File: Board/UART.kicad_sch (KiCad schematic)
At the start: 24 parts, among them IC31 MAX232, IC32 MAX232, IC33 UARTPLCC, IC34 7406N, IC35 74138N, X3 M09HPS

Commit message: ultipet 1.1a board
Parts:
- removed IC33: UARTPLCC, cbm_ultipet_v1:PLCC44, symbol cbm_ultipet_v1-eagle-import:UARTPLCC
- removed JP21, JP22, JP23, JP25: JP2E, cbm_ultipet_v1:JP2, symbol cbm_ultipet_v1-eagle-import:JP2E
- removed R103: 10k, cbm_ultipet_v1:0207_10, symbol cbm_ultipet_v1-eagle-import:R-EU_0207/10
- added unit 5 of IC34
- added IC6: TL16C752C, Package_QFP:TQFP-48_7x7mm_P0.5mm, symbol TL16C752C:TL16C752C
- added U$2: JP5, cbm_ultipet_v1:JP5, symbol cbm_ultipet_v1-eagle-import:JP5
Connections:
- net /SEL1 is gone; now on net GND: IC35.4 (G2A)
- net BCTS is gone; now on net LCTS: U$27.2
- net BSIN is gone; now on net LRX: U$27.4
- net /BIRQ: now also IC34.10 (O)
- net BA0: now also IC6.28 (A0)
- net BA1: now also IC6.27 (A1)
- net BA2: now also IC6.26 (A2)
- net BD0: now also IC6.44 (D0)
- net BD1: now also IC6.45 (D1)
- net BD2: now also IC6.46 (D2)
- net BD3: now also IC6.47 (D3)
- net BD4: now also IC6.48 (D4)
- net BD5: now also IC6.1 (D5)
- net BD6: now also IC6.2 (D6)
- net BD7: now also IC6.3 (D7)
- net GND: now also IC6.17 (GND), U$2.1
- net LCTS: now also IC6.38 (/CTSA)
- net LDCD: now also IC6.40 (/CDA)
- net LDSR: now also IC6.39 (/DSRA)
- net LDTR: now also IC6.34 (/DTRA)
- net LRTS: now also IC6.33 (/RTSA)
- net LRX: now also IC6.5 (RXA)
- net LTX: now also IC6.7 (TXA)
- net VCC: now also IC6.42 (VCC)
- net PULLUP_UART: now reaches IC34.4 (O)
- net PULLUP_UART: now also IC6.36 (RESET)
- net /QRD: now reaches IC35.11 (Y4)
- net /QRD: now also IC6.15 (/IOW)
- net /QWR: now reaches IC35.10 (Y5)
- net /QWR: now also IC6.19 (/IOR)
- net at IC34.1 (I): now also IC6.30 (INTA)
- net SERCLK: no longer names the net of QG3.8 (OUT)
- net SERCLK: now also IC6.13 (XTALI)
- new net: IC34.11 (I), IC6.29 (INTB)
- new net OPENHIGH: IC6.16 (/CDB), IC6.20 (/DSRB), IC6.21 (/RIB), IC6.41 (/RIA)
- new net RCTS: IC6.23 (/CTSB), U$2.2
- new net RRTS: IC6.22 (/RTSB), U$2.5
- new net RRX: IC6.4 (RXB), U$2.4
- new net RTX: IC6.8 (TXB), U$2.3
- new net /SEL1: IC6.10 (/CSA)
- new net /SEL2: IC6.11 (/CSB)
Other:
- note added: "$e818-$e81f $e828-$e82f"
- note added: "1.1A: - Switch to DUAL UART to provide 2nd 5V RS232 (shared w/ UEXT) - replace pullup on UART /RES with RN7"
- note added: "CBM-ULTIPET-V1.1A"
- note added: "CBM-ULTIPET-V1.1A-20240525"
- note added: "RS232<->USB breakout board connector - Do not use if UEXT is used!"
- note added: "RS232<->USB breakout board connector - Remove MAX232 if used!"
- note removed: "$e818-$e81f"
- note removed: "- Changed UART to PLCC as DIP is unobtainable"
- note removed: "CBM-ULTIPET-V1.0A"
- note removed: "CBM-ULTIPET-V1.0A-20240122"
- note removed: "RS232<->USB breakout board connector"
- moved on the sheet: C134, C135, C137, C139, C84, C86, C87, C88, C89, C90, C91, IC31A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

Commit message: diverse fixes
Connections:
- net GND: now also IC6.16 (/CDB), IC6.20 (/DSRB)
- net OPENHIGH: no longer IC6.16 (/CDB), IC6.20 (/DSRB)
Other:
- note added: "1.1A: - Switch to DUAL UART to provide 2nd 5V RS232 (shared w/ UEXT) - replace pullup on UART /RES with RN7 1.2A: - set /DSRB and /CDB to lo instead of hi"
- note added: "CBM-ULTIPET-V1.2A"
- note added: "CBM-ULTIPET-V1.2A-20241010"
- note removed: "1.1A: - Switch to DUAL UART to provide 2nd 5V RS232 (shared w/ UEXT) - replace pullup on UART /RES with RN7"
- note removed: "CBM-ULTIPET-V1.1A"
- note removed: "CBM-ULTIPET-V1.1A-20240525"
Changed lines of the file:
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@@
 	)
 	(junction
+		(at 220.98 179.07)
+		(diameter 0)
+		(color 0 0 0 0)
+	)
+	(junction
 		(at 269.24 176.53)
 		(diameter 0)
@@
 	)
 	(junction
-		(at 217.17 173.99)
-		(diameter 0)
-		(color 0 0 0 0)
-	)
-	(junction
 		(at 273.05 40.64)
 		(diameter 0)
@@
 		(color 0 0 0 0)
 	)
-	(junction
-		(at 217.17 179.07)
-		(diameter 0)
-		(color 0 0 0 0)
-	)
 	(bus_entry
 		(at 153.67 143.51)
@@
 	(wire
 		(pts
-			(xy 217.17 181.61) (xy 217.17 179.07)
+			(xy 220.98 179.07) (xy 220.98 194.31)
+		)
+		(stroke
+			(width 0)
+			(type default)
+		)
+	)
+	(wire
+		(pts
+			(xy 217.17 168.91) (xy 217.17 181.61)
 		)
 		(stroke
@@
 	(wire
 		(pts
-			(xy 217.17 179.07) (xy 217.17 173.99)
-		)
-		(stroke
-			(width 0)
-			(type default)
-		)
-	)
-	(wire
-		(pts
 			(xy 298.45 96.52) (xy 280.67 96.52)
 		)
@@
 	(wire
 		(pts
+			(xy 208.28 179.07) (xy 220.98 179.07)
+		)
+		(stroke
+			(width 0)
+			(type default)
+		)
+	)
+	(wire
+		(pts
 			(xy 288.29 71.12) (xy 288.29 58.42)
 		)
@@
 	(wire
 		(pts
+			(xy 220.98 173.99) (xy 220.98 179.07)
+		)
+		(stroke
+			(width 0)
+			(type default)
+		)
+	)
+	(wire
+		(pts
 			(xy 219.71 71.12) (xy 227.33 71.12)
 		)
@@
 		)
 	)
-	(wire
-		(pts
-			(xy 217.17 173.99) (xy 217.17 168.91)
-		)
-		(stroke
-			(width 0)
-			(type default)
-		)
-	)
 	(bus
 		(pts
@@
 	(wire
 		(pts
-			(xy 208.28 173.99) (xy 217.17 173.99)
-		)
-		(stroke
-			(width 0)
-			(type default)
-		)
-	)
-	(wire
-		(pts
 			(xy 227.33 38.1) (xy 227.33 40.64)
 		)
@@
 		)
 	)
-	(wire
-		(pts
-			(xy 208.28 179.07) (xy 217.17 179.07)
-		)
-		(stroke
-			(width 0)
-			(type default)
-		)
-	)
 	(bus
 		(pts
@@
 	(wire
 		(pts
+			(xy 208.28 173.99) (xy 220.98 173.99)
+		)
+		(stroke
+			(width 0)
+			(type default)
+		)
+	)
+	(wire
+		(pts
 			(xy 86.36 214.63) (xy 104.14 214.63)
 		)
@@
 		)
 	)
-	(text "CBM-ULTIPET-V1.1A\n"
+	(text "CBM-ULTIPET-V1.2A\n"
 		(exclude_from_sim no)
 		(at 294.64 224.028 0)
@@
 		)
 	)
-	(text "CBM-ULTIPET-V1.1A-20240525"
+	(text "CBM-ULTIPET-V1.2A-20241010"
 		(exclude_from_sim no)
 		(at 303.276 243.84 0)
@@
 		)
 	)
-	(text "1.1A:\n- Switch to DUAL UART to provide 2nd\n  5V RS232 (shared w/ UEXT)\n- replace pullup on UART /RES \n  with RN7"
+	(text "1.1A:\n- Switch to DUAL UART to provide 2nd\n  5V RS232 (shared w/ UEXT)\n- replace pullup on UART /RES \n  with RN7\n1.2A:\n- set /DSRB and /CDB to lo instead of hi"
 		(exclude_from_sim no)
-		(at 310.896 141.986 0)
+		(at 300.482 144.018 0)
 		(effects
 			(font
@@
 					(unit 1)
 				)
+			)
+		)
+	)
+	(symbol
+		(lib_id "cbm_ultipet_v1-eagle-import:GND")
+		(at 220.98 196.85 0)
+		(unit 1)
+		(exclude_from_sim no)
+		(in_bom yes)
+		(on_board yes)
+		(dnp no)
+		(property "Reference" "#GND0143"
+			(at 220.98 196.85 0)
+			(effects
+				(font
+					(size 1.27 1.27)
+				)
+				(hide yes)
+			)
+		)
+		(property "Value" "GND"
+			(at 218.44 199.39 0)
+			(effects
+				(font
+					(size 1.778 1.5113)
+				)
+				(justify left bottom)
+			)
+		)
+		(property "Footprint" ""
+			(at 220.98 196.85 0)
+			(effects
+				(font
+					(size 1.27 1.27)
+				)
+				(hide yes)
+			)
+		)
+		(property "Datasheet" ""
+			(at 220.98 196.85 0)
+			(effects
+				(font
+					(size 1.27 1.27)
+				)
+				(hide yes)
+			)
+		)
+		(property "Description" ""
+			(at 220.98 196.85 0)
+			(effects
+				(font
+					(size 1.27 1.27)
+				)
+				(hide yes)
+			)
+		)
+		(pin "1"
+		)
+		(instances
+			(project "cbm_ultipet_v1"
+				(path "/4dd2dd78-173f-4b46-8cce-4ed940435c94/511b245b-0d04-40fa-b689-60e442c438dc"
+					(reference "#GND0143")
+					(unit 1)
+				)

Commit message: various fixes as documented in github issues
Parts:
- added R12, R5: 10k, cbm_ultipet_v1:0207_10, symbol cbm_ultipet_v1-eagle-import:R-EU_0207/10
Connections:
- net GND: now also R12.1, R5.1
- net at IC34.1 (I), IC6.30 (INTA): now also R12.2
- net at IC34.11 (I), IC6.29 (INTB): now also R5.2
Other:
- note added: "1.1A: - Switch to DUAL UART to provide 2nd 5V RS232 (shared w/ UEXT) - replace pullup on UART /RES with RN7 1.2A: - set /DSRB and /CDB to lo instead of hi . add pulldowns to INTA and INTB so high-Z does not trigger IRQ"
- note added: "CBM-ULTIPET-V1.2A-20241013"
- note removed: "1.1A: - Switch to DUAL UART to provide 2nd 5V RS232 (shared w/ UEXT) - replace pullup on UART /RES with RN7 1.2A: - set /DSRB and /CDB to lo instead of hi"
- note removed: "CBM-ULTIPET-V1.2A-20241010"

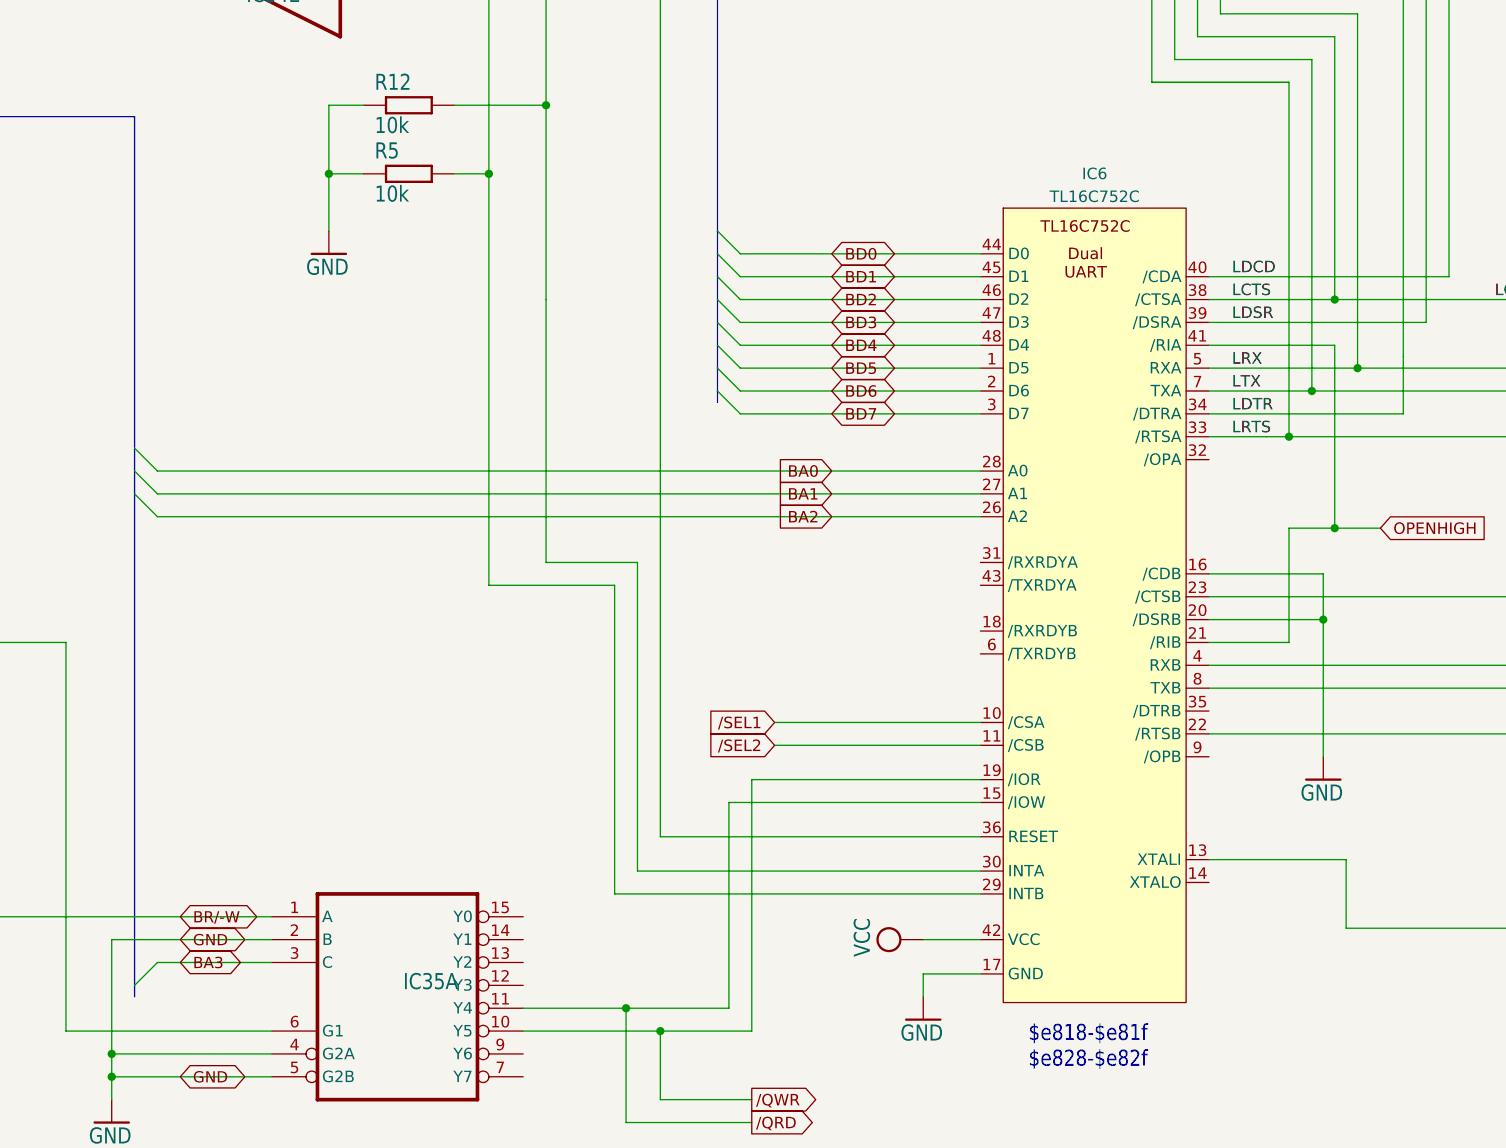
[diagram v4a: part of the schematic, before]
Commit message: replace some ultipet specific TQFP with easier to solder parts
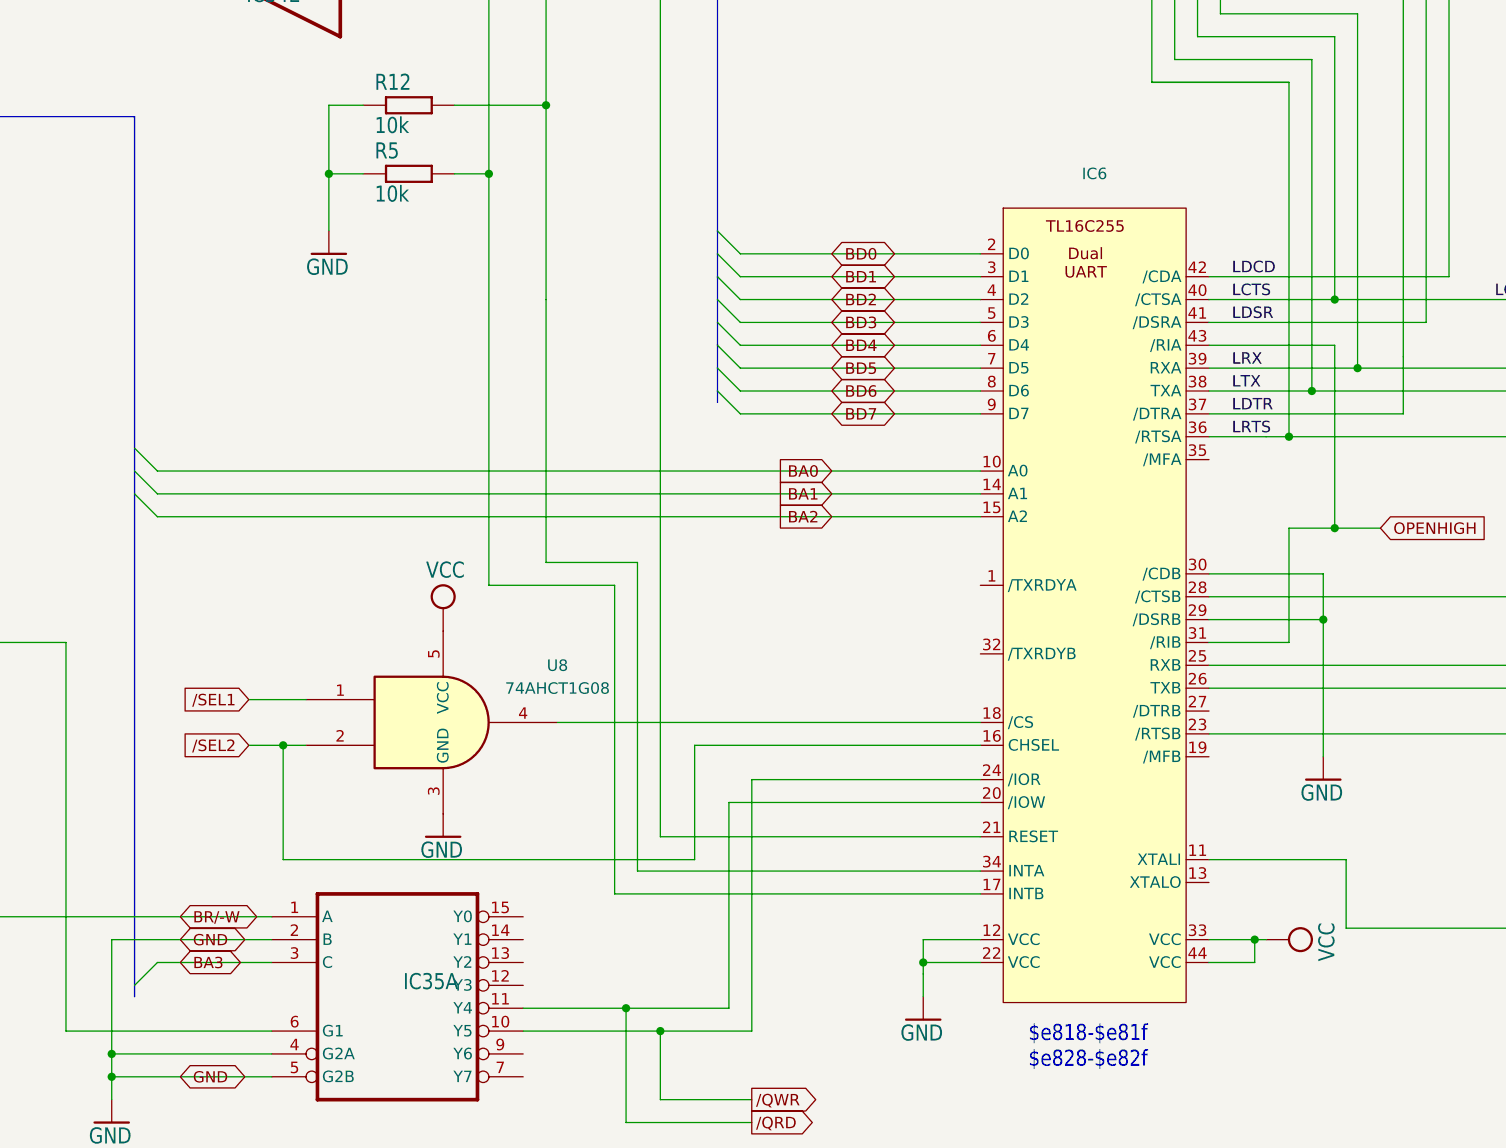
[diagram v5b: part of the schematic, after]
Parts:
- removed IC6: TL16C752C, Package_QFP:TQFP-48_7x7mm_P0.5mm, symbol TL16C752C:TL16C752C
- added IC6: ~, Package_LCC:PLCC-44_THT-Socket, symbol TL16C752C:TL16C255
- added U8: 74AHCT1G08, Package_SO:TSOP-5_1.65x3.05mm_P0.95mm, symbol 74xGxx:74AHCT1G08
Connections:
- net BA0: now also IC6.10 (A0)
- net BA1: now also IC6.14 (A1)
- net BA2: now also IC6.15 (A2)
- net BD0: now also IC6.2 (D0)
- net BD1: now also IC6.3 (D1)
- net BD2: now also IC6.4 (D2)
- net BD3: now also IC6.5 (D3)
- net BD4: now also IC6.6 (D4)
- net BD5: now also IC6.7 (D5)
- net BD6: now also IC6.8 (D6)
- net BD7: now also IC6.9 (D7)
- net GND: now also IC6.12 (VCC), IC6.22 (VCC), IC6.29 (/DSRB), IC6.30 (/CDB), U8.3 (GND)
- net LCTS: now also IC6.40 (/CTSA)
- net LDCD: now also IC6.42 (/CDA)
- net LDSR: now also IC6.41 (/DSRA)
- net LDTR: now also IC6.37 (/DTRA)
- net LRTS: now also IC6.36 (/RTSA)
- net LRX: now also IC6.39 (RXA)
- net LTX: now also IC6.38 (TXA)
- net OPENHIGH: now also IC6.31 (/RIB), IC6.43 (/RIA)
- net PULLUP_UART: now also IC6.21 (RESET)
- net RCTS: now also IC6.28 (/CTSB)
- net RRTS: now also IC6.23 (/RTSB)
- net RRX: now also IC6.25 (RXB)
- net RTX: now also IC6.26 (TXB)
- net VCC: now also IC6.33 (VCC), IC6.44 (VCC), U8.5 (VCC)
- net /QRD: now also IC6.20 (/IOW)
- net /QWR: now also IC6.24 (/IOR)
- net /SEL1: now also U8.1
- net /SEL2: now also IC6.16 (CHSEL), U8.2
- net at IC34.11 (I), R5.2: now also IC6.17 (INTB)
- net at QG3.8 (OUT): now also IC6.11 (XTALI)
- net at IC34.1 (I), R12.2: now also IC6.34 (INTA)
- new net: IC6.18 (/CS), U8.4

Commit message: work on 1.3
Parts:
- IC31, IC32, IC35: footprint cbm_ultipet_v1:DIL16 -> Package_DIP:DIP-16_W7.62mm_Socket_LongPads
- IC34: footprint cbm_ultipet_v1:DIL14 -> Package_DIP:DIP-14_W7.62mm_Socket_LongPads
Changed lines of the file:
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@@
 (kicad_sch
-	(version 20231120)
+	(version 20250114)
 	(generator "eeschema")
-	(generator_version "8.0")
+	(generator_version "9.0")
 	(paper "User" 400 271.932)
+	(text "CBM-ULTIPET-V1.2A\n"
+		(exclude_from_sim no)
+		(at 294.64 224.028 0)
+		(effects
+			(font
+				(size 3.81 3.2385)
+			)
+			(justify left bottom)
+		)
+	)
+	(text "RS232<->USB\nbreakout board\nconnector -\nDo not use if\nUEXT is used!\n"
+		(exclude_from_sim no)
+		(at 264.16 156.464 0)
+		(effects
+			(font
+				(size 1.778 1.5113)
+			)
+			(justify left bottom)
+		)
+	)
+	(text "$e818-$e81f\n$e828-$e82f"
+		(exclude_from_sim no)
+		(at 188.214 229.108 0)
+		(effects
+			(font
+				(size 1.778 1.5113)
+			)
+			(justify left bottom)
+		)
+	)
+	(text "CBM-ULTIPET-V1.2A-20241013\n"
+		(exclude_from_sim no)
+		(at 303.276 243.84 0)
+		(effects
+			(font
+				(size 1.778 1.5113)
+			)
+			(justify left bottom)
+		)
+	)
+	(text "1.1A:\n- Switch to DUAL UART to provide 2nd\n  5V RS232 (shared w/ UEXT)\n- replace pullup on UART /RES \n  with RN7\n1.2A:\n- set /DSRB and /CDB to lo instead of hi\n. add pulldowns to INTA and INTB so high-Z\n  does not trigger IRQ"
+		(exclude_from_sim no)
+		(at 300.482 144.018 0)
+		(effects
+			(font
+				(size 2.54 2.54)
+			)
+			(justify left)
+		)
+	)
+	(text "RS232<->USB\nbreakout board\nconnector -\nRemove MAX232\nif used!\n"
+		(exclude_from_sim no)
+		(at 244.856 122.428 0)
+		(effects
+			(font
+				(size 1.778 1.5113)
+			)
+			(justify left bottom)
+		)
+	)
 	(junction
 		(at 105.41 193.04)
@@
 		)
 	)
-	(text "CBM-ULTIPET-V1.2A\n"
-		(exclude_from_sim no)
-		(at 294.64 224.028 0)
-		(effects
-			(font
-				(size 3.81 3.2385)
-			)
-			(justify left bottom)
-		)
-	)
-	(text "RS232<->USB\nbreakout board\nconnector -\nDo not use if\nUEXT is used!\n"
-		(exclude_from_sim no)
-		(at 264.16 156.464 0)
-		(effects
-			(font
-				(size 1.778 1.5113)
-			)
-			(justify left bottom)
-		)
-	)
-	(text "$e818-$e81f\n$e828-$e82f"
-		(exclude_from_sim no)
-		(at 188.214 229.108 0)
-		(effects
-			(font
-				(size 1.778 1.5113)
-			)
-			(justify left bottom)
-		)
-	)
-	(text "CBM-ULTIPET-V1.2A-20241013\n"
-		(exclude_from_sim no)
-		(at 303.276 243.84 0)
-		(effects
-			(font
-				(size 1.778 1.5113)
-			)
-			(justify left bottom)
-		)
-	)
-	(text "1.1A:\n- Switch to DUAL UART to provide 2nd\n  5V RS232 (shared w/ UEXT)\n- replace pullup on UART /RES \n  with RN7\n1.2A:\n- set /DSRB and /CDB to lo instead of hi\n. add pulldowns to INTA and INTB so high-Z\n  does not trigger IRQ"
-		(exclude_from_sim no)
-		(at 300.482 144.018 0)
-		(effects
-			(font
-				(size 2.54 2.54)
-			)
-			(justify left)
-		)
-	)
-	(text "RS232<->USB\nbreakout board\nconnector -\nRemove MAX232\nif used!\n"
-		(exclude_from_sim no)
-		(at 244.856 122.428 0)
-		(effects
-			(font
-				(size 1.778 1.5113)
-			)
-			(justify left bottom)
-		)
-	)
 	(label "LDSR"
 		(at 210.82 146.05 0)
@@
 			)
 		)
-		(property "Footprint" "cbm_ultipet_v1:DIL16"
+		(property "Footprint" "Package_DIP:DIP-16_W7.62mm_Socket_LongPads"
 			(at 252.73 86.36 0)
 			(effects
@@
 			)
 		)
-		(property "Footprint" "cbm_ultipet_v1:DIL16"
+		(property "Footprint" "Package_DIP:DIP-16_W7.62mm_Socket_LongPads"
 			(at 97.79 38.1 0)
 			(effects
@@
 			)
 		)
-		(property "Footprint" "cbm_ultipet_v1:DIL16"
+		(property "Footprint" "Package_DIP:DIP-16_W7.62mm_Socket_LongPads"
 			(at 119.38 219.71 0)
 			(effects
@@
 			)
 		)
-		(property "Footprint" "cbm_ultipet_v1:DIL14"
+		(property "Footprint" "Package_DIP:DIP-14_W7.62mm_Socket_LongPads"
 			(at 107.95 38.1 0)
 			(effects
@@
 			)
 		)
-		(property "Footprint" "cbm_ultipet_v1:DIL16"
+		(property "Footprint" "Package_DIP:DIP-16_W7.62mm_Socket_LongPads"
 			(at 118.11 38.1 0)
 			(effects
@@
 			)
 		)
-		(property "Footprint" "cbm_ultipet_v1:DIL14"
+		(property "Footprint" "Package_DIP:DIP-14_W7.62mm_Socket_LongPads"
 			(at 106.68 92.71 0)
 			(effects
@@
 			)
 		)
-		(property "Footprint" "cbm_ultipet_v1:DIL14"
+		(property "Footprint" "Package_DIP:DIP-14_W7.62mm_Socket_LongPads"
 			(at 104.14 80.01 0)
 			(effects
@@
 			)
 		)
-		(property "Footprint" "cbm_ultipet_v1:DIL16"
+		(property "Footprint" "Package_DIP:DIP-16_W7.62mm_Socket_LongPads"
 			(at 87.63 38.1 0)
 			(effects
@@
 			)
 		)
-		(property "Footprint" "cbm_ultipet_v1:DIL16"
+		(property "Footprint" "Package_DIP:DIP-16_W7.62mm_Socket_LongPads"
 			(at 250.19 43.18 0)
 			(effects
@@
 			)
 		)
-		(property "Footprint" "cbm_ultipet_v1:DIL14"
+		(property "Footprint" "Package_DIP:DIP-14_W7.62mm_Socket_LongPads"
 			(at 106.68 109.22 0)
 			(effects
